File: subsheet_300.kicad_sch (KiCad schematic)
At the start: 7 parts, among them U300_DIP40 ST_DMA_DIP40_PHY, U300_PLCC44 ST_DMA_PLCC44_PHY

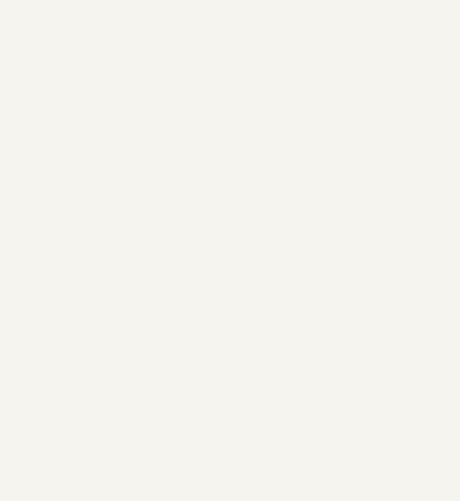
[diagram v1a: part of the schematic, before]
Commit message: add gnd/vcc symbol to start replacing local labels
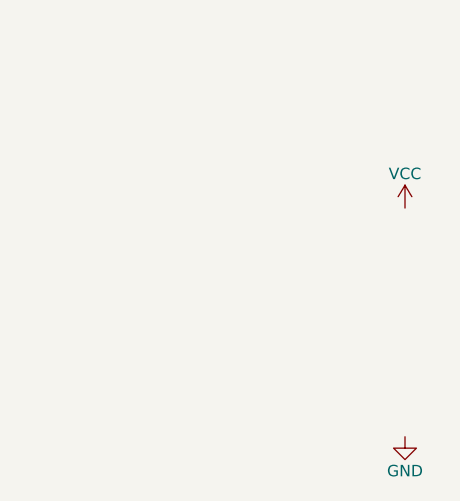
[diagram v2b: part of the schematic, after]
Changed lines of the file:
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@@
     (pin "8")
   )
+  (symbol (lib_id "power:VCC") (at 184.15 212.09 0) (unit 1)
+    (in_bom yes) (on_board yes)
+    (property "Reference" "#PWR?" (id 0) (at 184.15 215.9 0)
+      (effects (font (size 1.27 1.27)) hide)
+    )
+    (property "Value" "VCC" (id 1) (at 184.15 208.28 0))
+    (property "Footprint" "" (id 2) (at 184.15 212.09 0)
+      (effects (font (size 1.27 1.27)) hide)
+    )
+    (property "Datasheet" "" (id 3) (at 184.15 212.09 0)
+      (effects (font (size 1.27 1.27)) hide)
+    )
+    (pin "1")
+  )
+  (symbol (lib_id "power:GND") (at 184.15 237.49 0) (unit 1)
+    (in_bom yes) (on_board yes)
+    (property "Reference" "#PWR?" (id 0) (at 184.15 243.84 0)
+      (effects (font (size 1.27 1.27)) hide)
+    )
+    (property "Value" "GND" (id 1) (at 184.15 241.3 0))
+    (property "Footprint" "" (id 2) (at 184.15 237.49 0)
+      (effects (font (size 1.27 1.27)) hide)
+    )
+    (property "Datasheet" "" (id 3) (at 184.15 237.49 0)
+      (effects (font (size 1.27 1.27)) hide)
+    )
+    (pin "1")
+  )
 )
